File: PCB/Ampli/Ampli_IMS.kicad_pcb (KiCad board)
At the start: 2 copper layers, 65 x 32 mm, 22 parts, among them J1 5227161-3, J2 5227161-3, J3 Conn_01x03_Male, SW1 SS22D0205G2, U1 ADA4625-1, U2 LT1464CS8

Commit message: Low noise smd amp
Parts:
- removed the R2 at (35.0, 29.0)
- removed R7: 6.65K MF 1/2W, Resistor_THT:R_Axial_DIN0204_L3.6mm_D1.6mm_P5.08mm_Horizontal
- C3: renamed from C2; footprint Capacitor_THT:C_Disc_D3.8mm_W2.6mm_P2.50mm -> Capacitor_SMD:C_0805_2012Metric
- C4: renamed from C6; footprint Capacitor_THT:C_Disc_D3.8mm_W2.6mm_P2.50mm -> Capacitor_SMD:C_0805_2012Metric
- C5: renamed from C3; footprint Capacitor_THT:C_Disc_D3.8mm_W2.6mm_P2.50mm -> Capacitor_SMD:C_0805_2012Metric
- C6: renamed from C7; footprint Capacitor_THT:C_Disc_D3.8mm_W2.6mm_P2.50mm -> Capacitor_SMD:C_0805_2012Metric
- C7: renamed from C5; value C_Small -> 100pF; footprint Capacitor_THT:C_Disc_D3.8mm_W2.6mm_P2.50mm -> Capacitor_SMD:C_0805_2012Metric
- J2: renamed from J1; footprint Connector_Coaxial:BNC_Amphenol_B6252HB-NPP3G-50_Horizontal -> Connector_Coaxial:SMA_Amphenol_132203-12_Horizontal
- R1: renamed from R3; footprint Resistor_THT:R_Axial_DIN0204_L3.6mm_D1.6mm_P5.08mm_Horizontal -> Capacitor_SMD:C_0805_2012Metric
- R2: renamed from R1; footprint Resistor_THT:R_Axial_DIN0204_L3.6mm_D1.6mm_P5.08mm_Horizontal -> Capacitor_SMD:C_0805_2012Metric
- R3: renamed from R4; footprint Resistor_THT:R_Axial_DIN0204_L3.6mm_D1.6mm_P5.08mm_Horizontal -> Capacitor_SMD:C_0805_2012Metric
- R4: renamed from R6; value 1.13K MF 1/4W -> 1K; footprint Resistor_THT:R_Axial_DIN0204_L3.6mm_D1.6mm_P5.08mm_Horizontal -> Capacitor_SMD:C_0805_2012Metric
- R5: footprint Resistor_THT:R_Axial_DIN0204_L3.6mm_D1.6mm_P5.08mm_Horizontal -> Capacitor_SMD:C_0805_2012Metric
- U1: value ADA4625-1 -> LMC6081
- moved C4 17.9 mm to (37.7, 37.1), turned to 0 degrees
- moved C5 14.9 mm to (44.1, 31.8)
- moved U1 11.5 mm to (39.3, 33.4), turned to 0 degrees
- moved R3 10.1 mm to (54.1, 45.3), turned to 0 degrees
- moved R1 8.64 mm to (34.6, 34.9), turned to 90 degrees
- moved R4 8.45 mm to (59.6, 41.3), turned to 90 degrees
- moved R2 5.65 mm to (45.7, 43.1), turned to 270 degrees
- moved SW1 5.39 mm to (39.6, 40.9), turned to 270 degrees
- moved C3 5.03 mm to (52.3, 37.7), turned to 180 degrees
- moved U2 4.11 mm to (50.6, 41.6)
- moved C7 3.78 mm to (57.6, 41.3)
- moved C6 3.54 mm to (49.0, 45.4), turned to 0 degrees
- moved R5 2.70 mm to (55.4, 41.3)
- moved J2 2.08 mm to (29.0, 34.0)
- renumbered C4 to C2, J3 to J1, J2 to J3
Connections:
- net /+15V renamed /+5V
- net /-15V renamed /-5V
- J2 pad 1: Net-(J1-Pad1) -> Net-(J2-Pad1)
- R1 pad 2: Net-(R2-Pad1) (its old number) -> Net-(J2-Pad1)
- U1 pad 1: Net-(U1-Pad1) -> (no net)
- U1 pad 3: Net-(R2-Pad1) (its old number) -> Net-(J2-Pad1)
- U1 pad 5: Net-(U1-Pad5) -> (no net)
- U1 pad 8: Net-(U1-Pad8) -> (no net)
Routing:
- net /+5V: track 61.3 -> 33.9 mm
- net Net-(C7-Pad2): track 33.1 -> 6.42 mm
- net /-5V: track 47.6 -> 73.5 mm, vias 0 -> 2
- net Net-(R2-Pad1) (its old number): track 17.4 -> 0.00 mm
- net Net-(C7-Pad1): track 29.1 -> 38.5 mm
- net Net-(R2-Pad1): track 18.0 -> 8.99 mm
- net Net-(J2-Pad1): track 0.00 -> 7.73 mm
- net Net-(R1-Pad1): track 29.1 -> 21.8 mm
- net Net-(SW1-Pad4): track 20.1 -> 13.5 mm, vias 1 -> 0
- net Net-(J3-Pad1): track 41.6 -> 45.9 mm
- net Net-(J1-Pad1): track 4.15 -> 0.00 mm
- net GND: track 3.06 -> 0.00 mm
- net Net-(R3-Pad1): track 16.9 -> 16.3 mm
- added copper zone on F.Cu, net GND
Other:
- board size 65 x 32 mm -> 58.4 x 32 mm

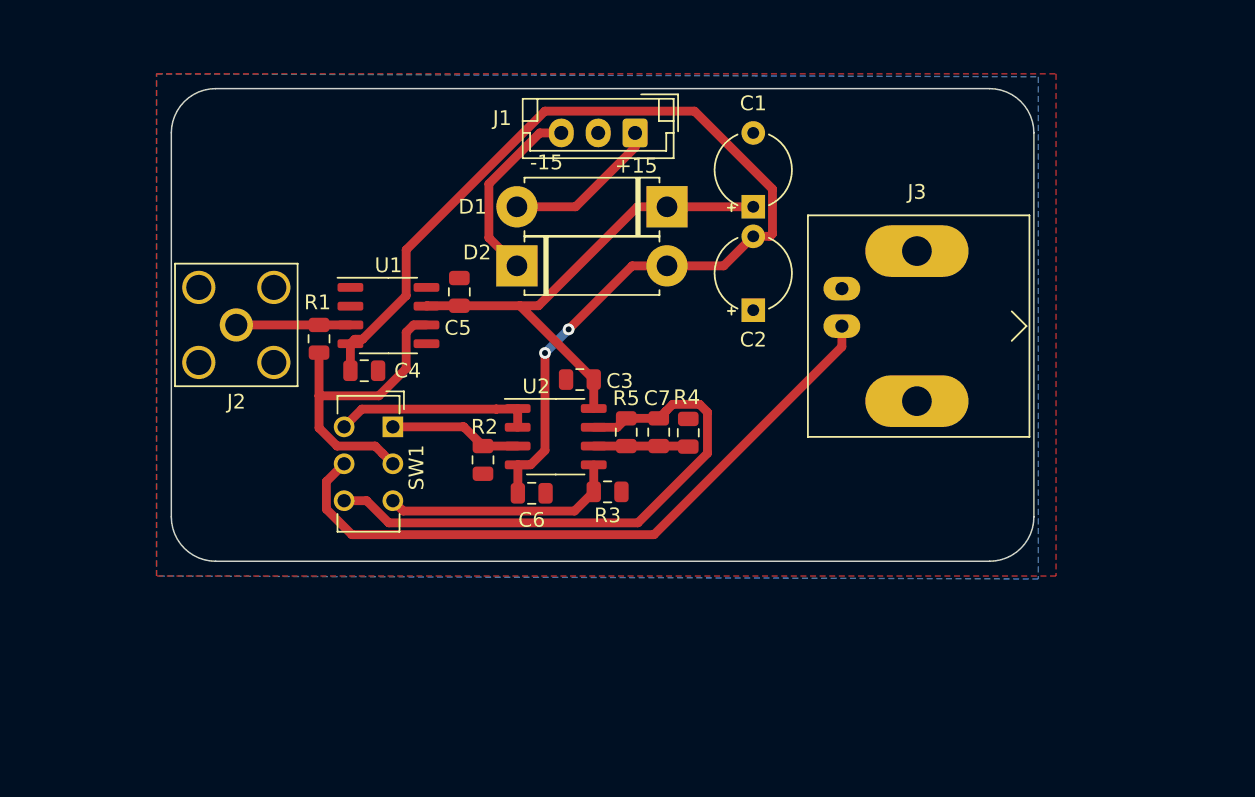
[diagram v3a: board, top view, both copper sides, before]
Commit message: SMD + low noise design
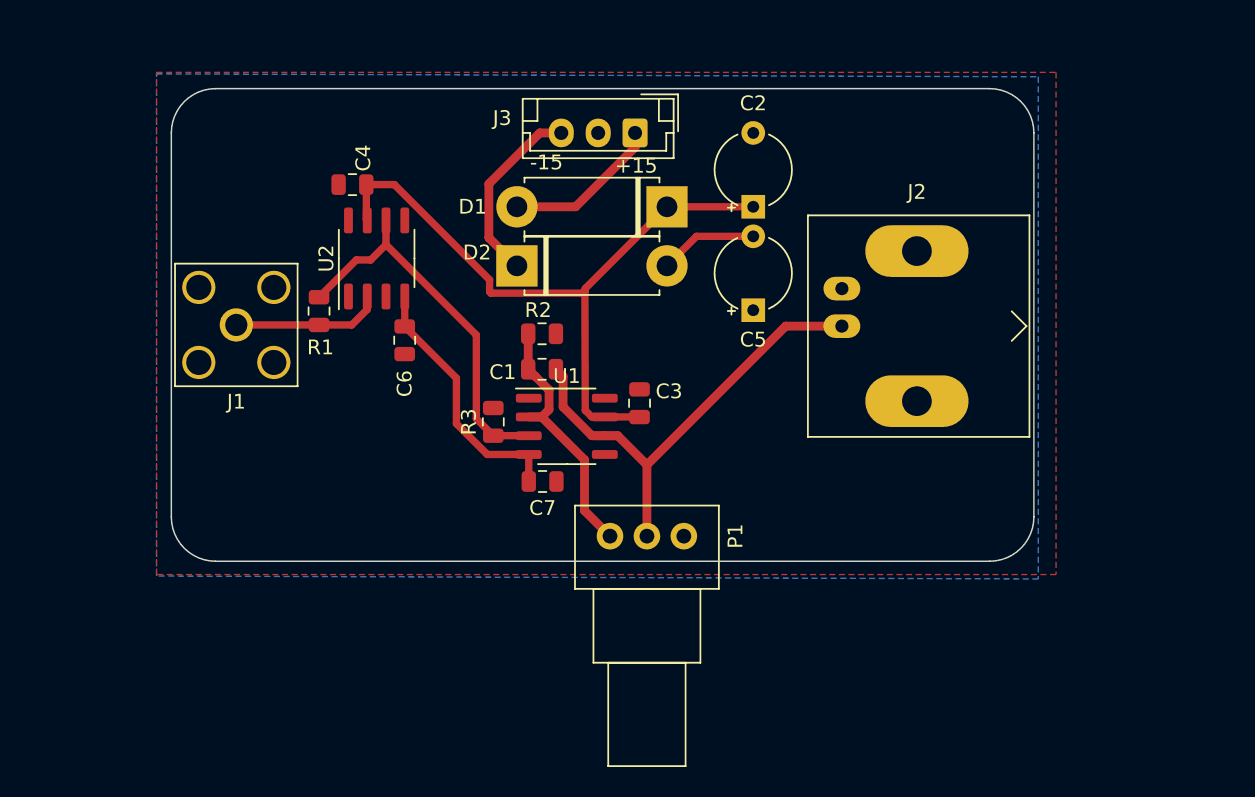
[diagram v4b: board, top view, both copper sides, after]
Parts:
- removed the R2 at (45.7, 43.1)
- removed R5: 9.09K MF 0.6W, Capacitor_SMD:C_0805_2012Metric
- removed SW1: SS22D0205G2, Button_Switch_THT:SW_CuK_JS202011CQN_DPDT_Straight
- removed the U2 at (50.6, 41.6)
- added P1: 300K, Potentiometer_THT:Potentiometer_Alps_RK09Y11_Single_Horizontal, F.Cu at (54.3, 48.3)
- added U1: LMC6081, Package_SO:SO-8_3.9x4.9mm_P1.27mm, F.Cu at (51.4, 40.9)
- R2: renamed from R4; value 1K -> 10K
- R3: value 10K MF 1/4W -> 10K
- moved R2 12.0 mm to (49.7, 34.6), turned to 0 degrees
- moved C4 10.3 mm to (36.9, 24.5), turned to 180 degrees
- moved R3 9.07 mm to (46.4, 40.6), turned to 90 degrees
- moved C1 8.98 mm to (49.7, 37.0), turned to 180 degrees
- moved C3 4.34 mm to (56.3, 39.3), turned to 90 degrees
- moved U2 3.95 mm to (38.5, 29.5), turned to 90 degrees
- moved C6 3.43 mm to (40.4, 35.0), turned to 270 degrees
- moved R1 1.88 mm to (34.6, 33.1), turned to 270 degrees
- moved C7 1.09 mm to (49.7, 44.6)
- renumbered C7 to C1, C1 to C2, C5 to C4, C2 to C5, C4 to C6, C6 to C7, J2 to J1, J3 to J2, J1 to J3, U1 to U2
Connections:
- C1 pad 1: Net-(C7-Pad1) -> Net-(C1-Pad1)
- J1 pad 1: Net-(J2-Pad1) -> Net-(J1-Pad1)
- J2 pad 1: Net-(J3-Pad1) -> Net-(C1-Pad1)
- R1 pad 2: Net-(J2-Pad1) -> Net-(J1-Pad1)
- R3 pad 1: Net-(R3-Pad1) -> Net-(R1-Pad1)
- U2 pad 2: GND -> Net-(J1-Pad1)
- U2 pad 3: Net-(J2-Pad1) -> GND
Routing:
- net /-5V: track 73.5 -> 24.3 mm, vias 2 -> 0
- net Net-(J3-Pad1): track 45.9 -> 0.00 mm
- net Net-(C7-Pad1): track 38.5 -> 0.00 mm
- net Net-(C1-Pad1): track 0.00 -> 32.0 mm
- net Net-(R3-Pad1): track 16.3 -> 0.00 mm
- net Net-(SW1-Pad4): track 13.5 -> 0.00 mm
- net /+5V: track 33.9 -> 46.6 mm
- net Net-(C1-Pad2): track 6.42 -> 17.3 mm
- net Net-(J1-Pad1): track 0.00 -> 10.2 mm
- net Net-(R2-Pad1): track 8.99 -> 0.00 mm
- net Net-(J2-Pad1): track 7.73 -> 0.00 mm
- net Net-(R1-Pad1): track 21.8 -> 26.0 mm

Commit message: low noise features
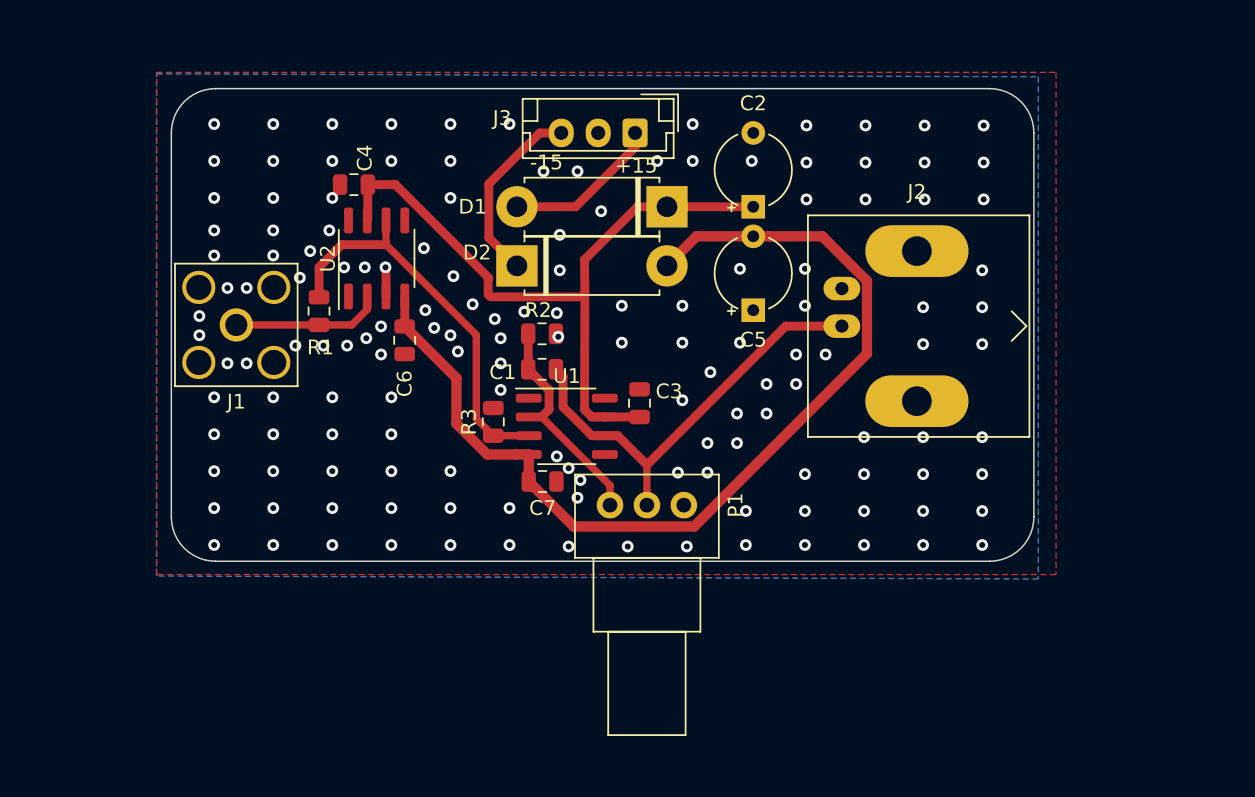
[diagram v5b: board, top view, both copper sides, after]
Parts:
- moved P1 2.10 mm to (54.3, 46.2)
- moved C4 0.10 mm to (37.0, 24.5)
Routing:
- net /-5V: track 24.3 -> 67.2 mm
- net Net-(C1-Pad1): track 32.0 -> 29.9 mm
- net Net-(C1-Pad2): track 17.3 -> 15.2 mm
- net GND: track 0.00 -> 2.04 mm, vias 0 -> 141
- net Net-(R1-Pad1): track 26.0 -> 27.2 mm
- net /+5V: track 46.6 -> 47.7 mm
- net (no net): vias 0 -> 5

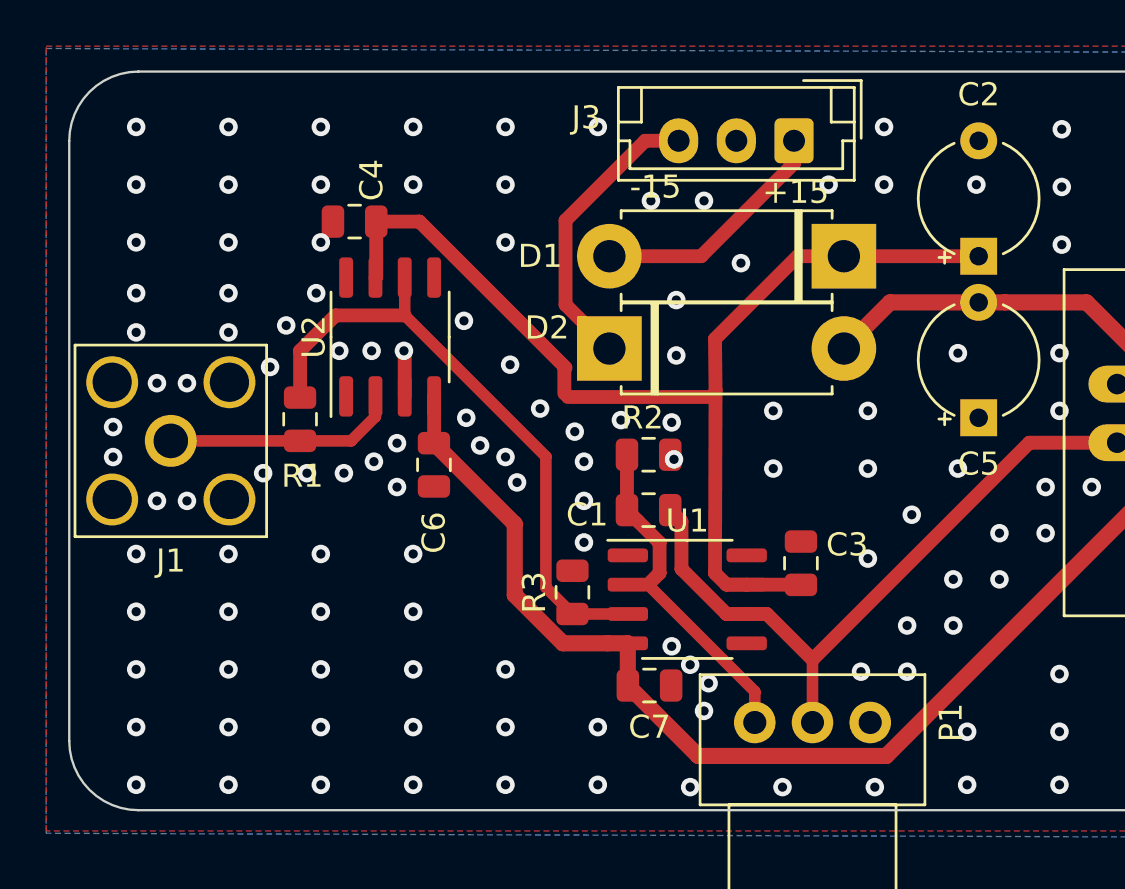
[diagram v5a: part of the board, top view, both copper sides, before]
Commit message: Small mistakes
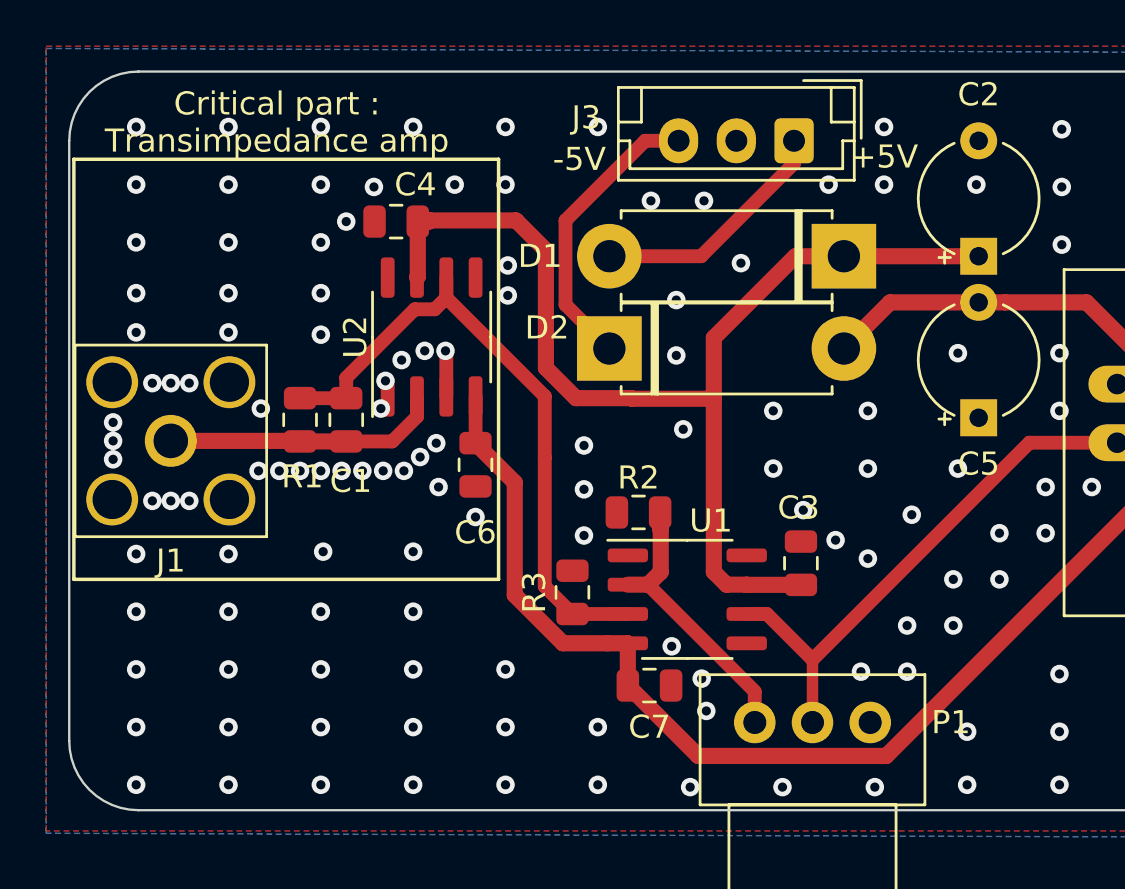
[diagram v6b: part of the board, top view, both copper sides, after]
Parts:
- C1: value 100pF -> 0.01pF
- moved C1 13.7 mm to (36.6, 33.1), turned to 270 degrees
- moved R2 2.54 mm to (49.3, 37.1), turned to 180 degrees
- moved C4 1.80 mm to (38.8, 24.5)
- moved C6 1.80 mm to (42.2, 35.0)
- moved U2 1.80 mm to (40.3, 29.5)
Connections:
- J1 pad 1: Net-(J1-Pad1) -> Net-(C1-Pad2)
- J2 pad 1: Net-(C1-Pad1) -> Net-(J2-Pad1)
- P1 pad 1: Net-(C1-Pad2) -> Net-(P1-Pad1)
- P1 pad 2: Net-(C1-Pad1) -> Net-(J2-Pad1)
- P1 pad 3: (no net) -> Net-(P1-Pad3)
- R1 pad 1: Net-(R1-Pad1) -> Net-(C1-Pad1)
- R1 pad 2: Net-(J1-Pad1) -> Net-(C1-Pad2)
- R2 pad 1: Net-(C1-Pad2) -> Net-(P1-Pad1)
- R3 pad 1: Net-(R1-Pad1) -> Net-(C1-Pad1)
- U1 pad 2: Net-(C1-Pad2) -> Net-(P1-Pad1)
- U1 pad 3: Net-(R1-Pad1) -> Net-(C1-Pad1)
- U1 pad 6: Net-(C1-Pad1) -> Net-(J2-Pad1)
- U2 pad 1: (no net) -> GND
- U2 pad 2: Net-(J1-Pad1) -> Net-(C1-Pad2)
- U2 pad 6: Net-(R1-Pad1) -> Net-(C1-Pad1)
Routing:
- net Net-(R1-Pad1): track 27.2 -> 0.00 mm
- net Net-(J2-Pad1): track 0.00 -> 23.5 mm
- net Net-(P1-Pad1): track 0.00 -> 12.1 mm
- net Net-(J1-Pad1): track 10.2 -> 0.00 mm
- net Net-(C1-Pad2): track 15.2 -> 12.0 mm
- net Net-(C1-Pad1): track 29.9 -> 27.9 mm
- net /+5V: track 47.7 -> 48.6 mm
- net /-5V: track 67.2 -> 66.5 mm
- net GND: vias 141 -> 151
- net (no net): vias 5 -> 0
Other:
- board text added: "+5V"
- board text added: "-5V"
- board text added: "Critical part : Transimpedance amp"
- board text removed: "+15"
- board text removed: "-15"
